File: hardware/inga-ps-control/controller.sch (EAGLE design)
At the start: 10 parts, among them IC1 MEGA8-P

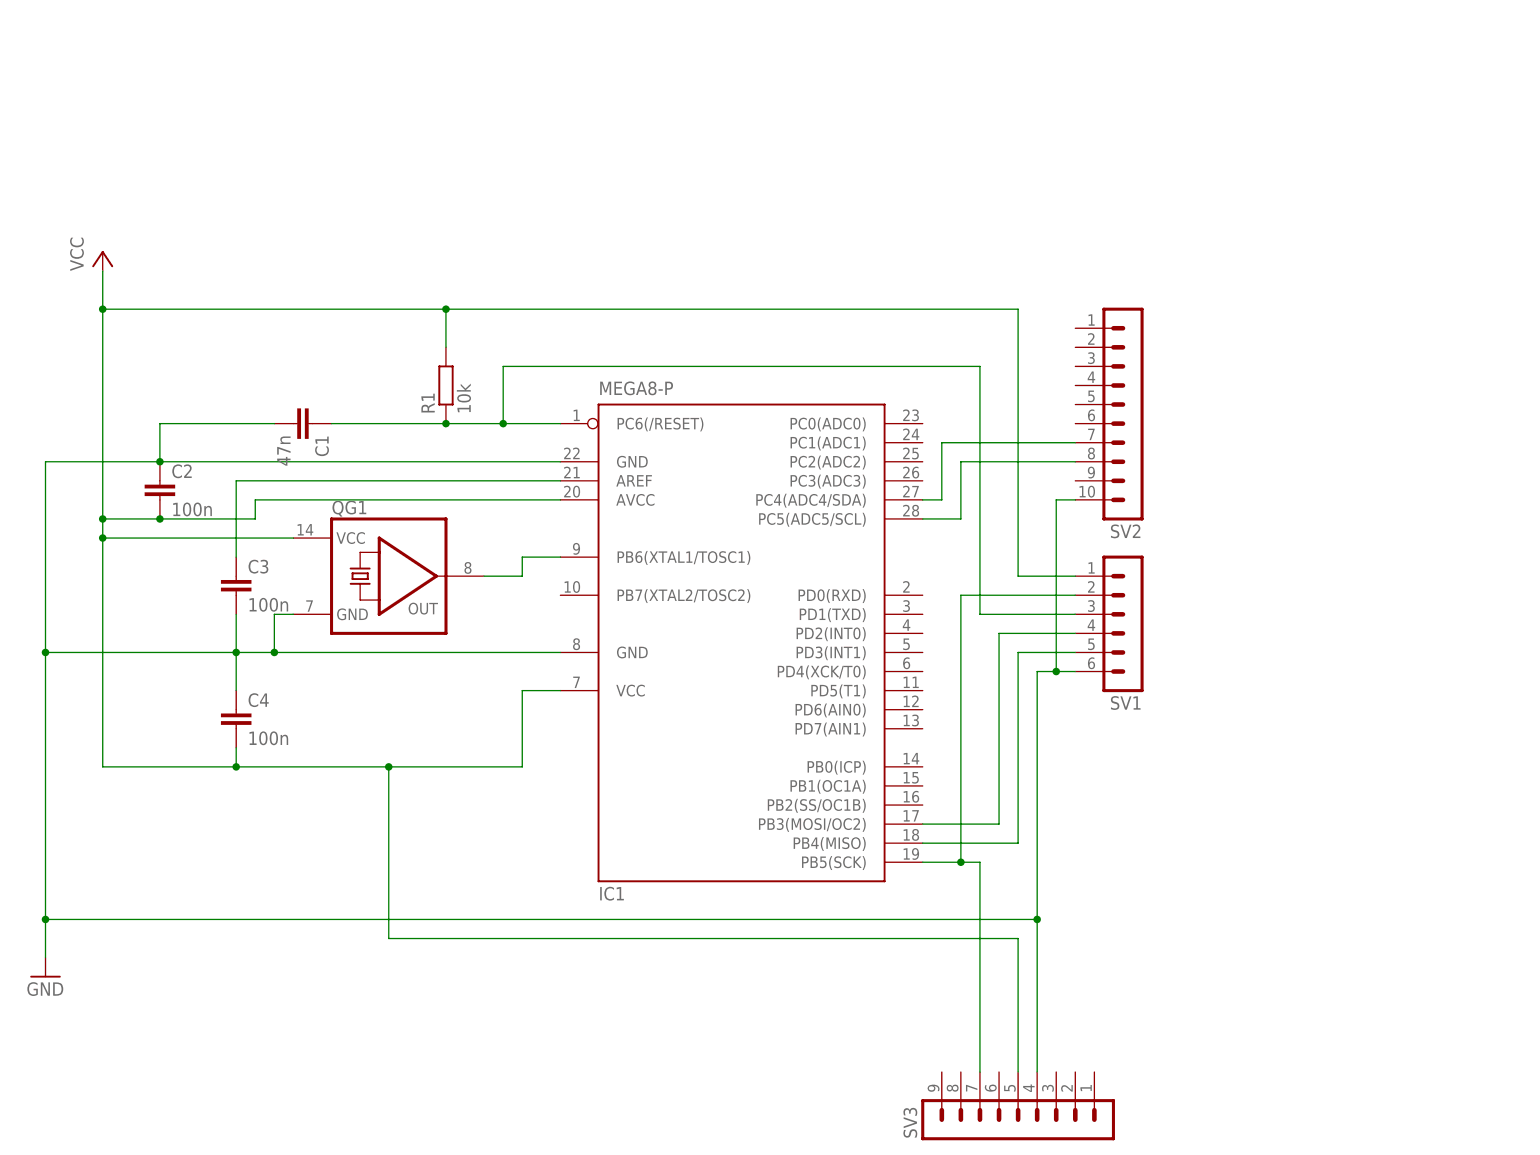
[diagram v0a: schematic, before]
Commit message: quarz statt oszillator
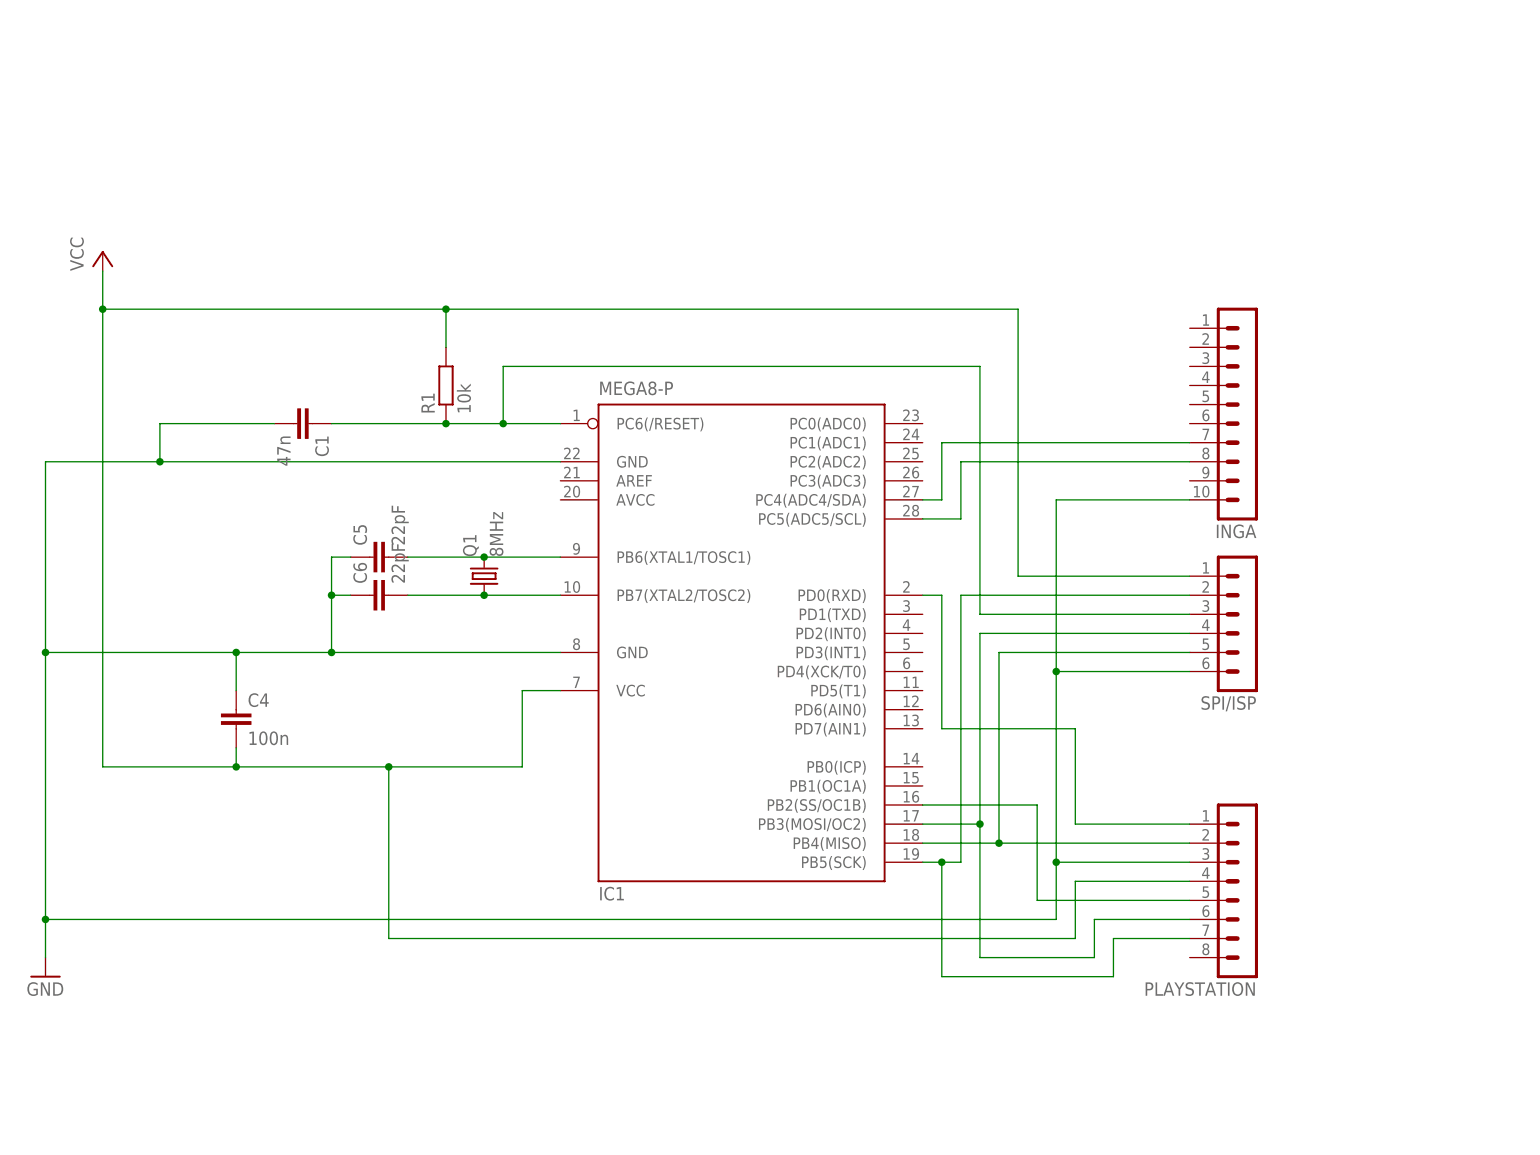
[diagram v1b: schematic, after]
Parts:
- removed C2, C3: 100n, capacitor-wima:C2,5-3
- removed QG1: (no value), crystal:QG5860
- removed SV1: (no value), con-lstb:MA06-1
- removed SV2: (no value), con-lstb:MA10-1
- removed SV3: (no value), con-lstb:MA09-1
- added C5, C6: 22pF, capacitor-wima:C2,5-3
- added INGA: (no value), con-lstb:MA10-1
- added PLAYSTATION: (no value), con-lstb:MA08-1
- added Q1: 8MHz, crystal:CRYSTALHC49U70
- added SPI/ISP: (no value), con-lstb:MA06-1
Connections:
- removed net N$4: C3.1, IC1.AREF
- new net N$10: IC1.PD0(RXD), PLAYSTATION.1
- new net N$5: C6.2, IC1.PB7(XTAL2/TOSC2), Q1.1
- new net PLAYSTATION: IC1.PB2(SS/OC1B), PLAYSTATION.5
- net GND: now also C5.1, C6.1, INGA.10, PLAYSTATION.3, SPI/ISP.6; no longer C2.1, C3.2, QG1.GND, SV1.6, SV2.10, SV3.4
- net N$1: now also C5.2, Q1.2; no longer QG1.OUT
- net N$2: now also SPI/ISP.3; no longer SV1.3
- net N$3: now also PLAYSTATION.7, SPI/ISP.2; no longer SV1.2, SV3.7
- net N$6: now also PLAYSTATION.6, SPI/ISP.4; no longer SV1.4
- net N$7: now also PLAYSTATION.2, SPI/ISP.5; no longer SV1.5
- net N$8: now also INGA.8; no longer SV2.8
- net N$9: now also INGA.7; no longer SV2.7
- net VCC: now also PLAYSTATION.4, SPI/ISP.1; no longer C2.2, IC1.AVCC, QG1.VCC, SV1.1, SV3.5

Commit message: schaltplan adapter
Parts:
- removed SPI/ISP: (no value), con-lstb:MA06-1
- added C2: 100nF, capacitor-wima:C2,5-3
- added INGA_SUPP: 22-23-2021, con-molex:22-23-2021
- added ISP: (no value), con-lstb:MA10-1
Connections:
- new net N$4: C2.2, IC1.AVCC
- net GND: now also C2.1, INGA_SUPP-2.S, ISP.10, ISP.4, ISP.6, ISP.8; no longer INGA.10, SPI/ISP.6
- net N$2: now also ISP.5; no longer SPI/ISP.3
- net N$3: now also ISP.7; no longer SPI/ISP.2
- net N$6: now also ISP.1; no longer SPI/ISP.4
- net N$7: now also ISP.9; no longer SPI/ISP.5
- net VCC: now also INGA_SUPP-1.S, ISP.2; no longer SPI/ISP.1
